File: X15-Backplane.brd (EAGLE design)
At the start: 160 x 100 mm, 34 parts, among them U1 ULN2003AD

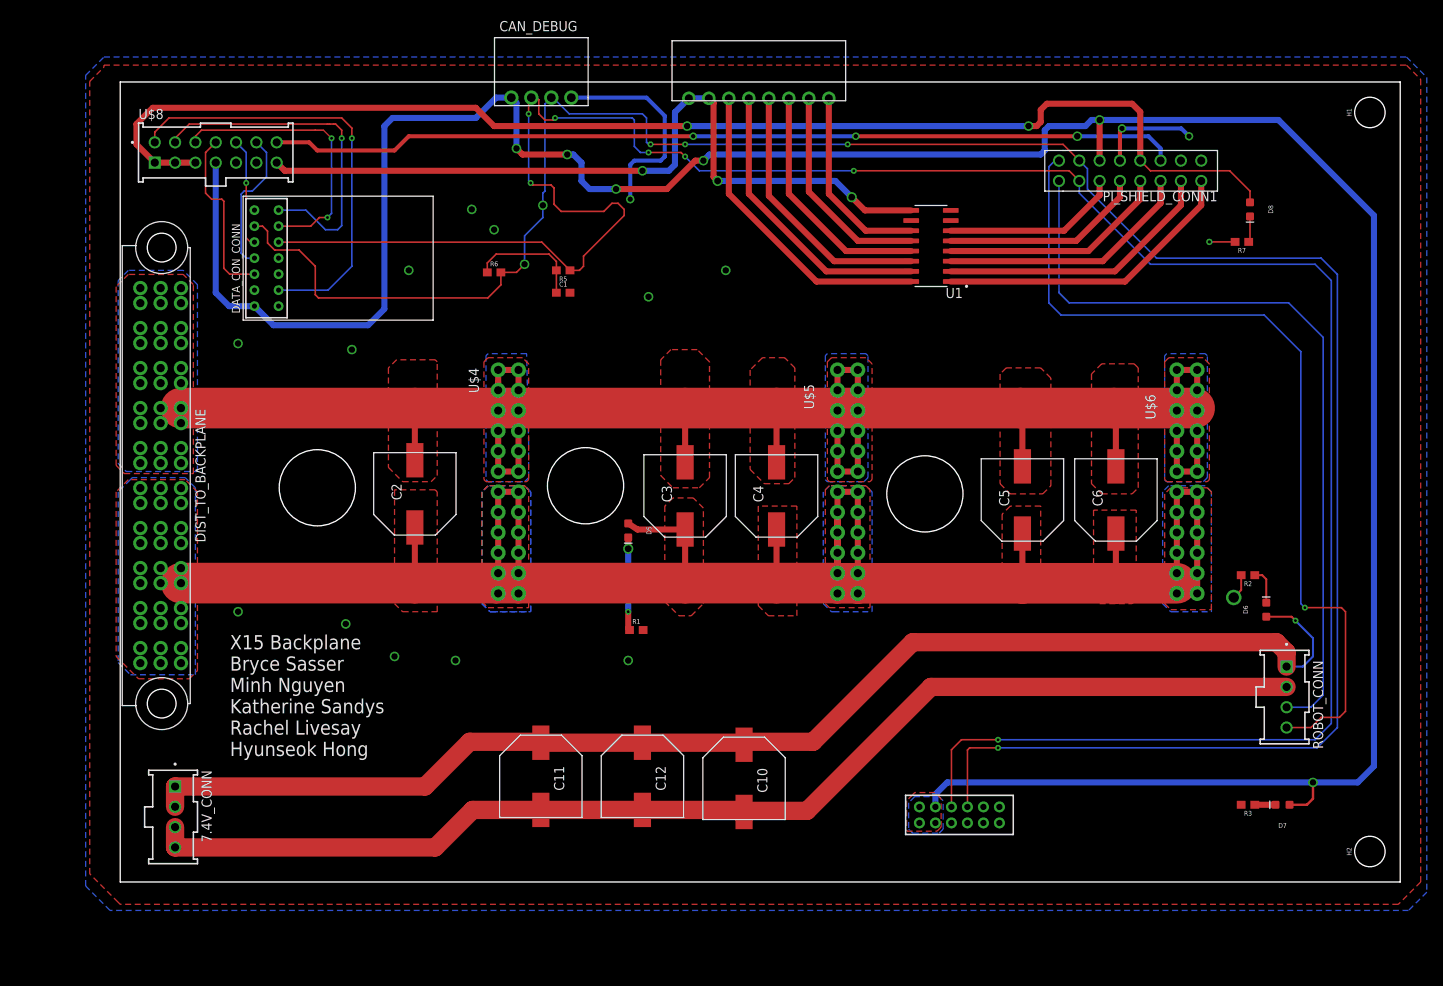
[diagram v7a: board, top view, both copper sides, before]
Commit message: fixed dimensions
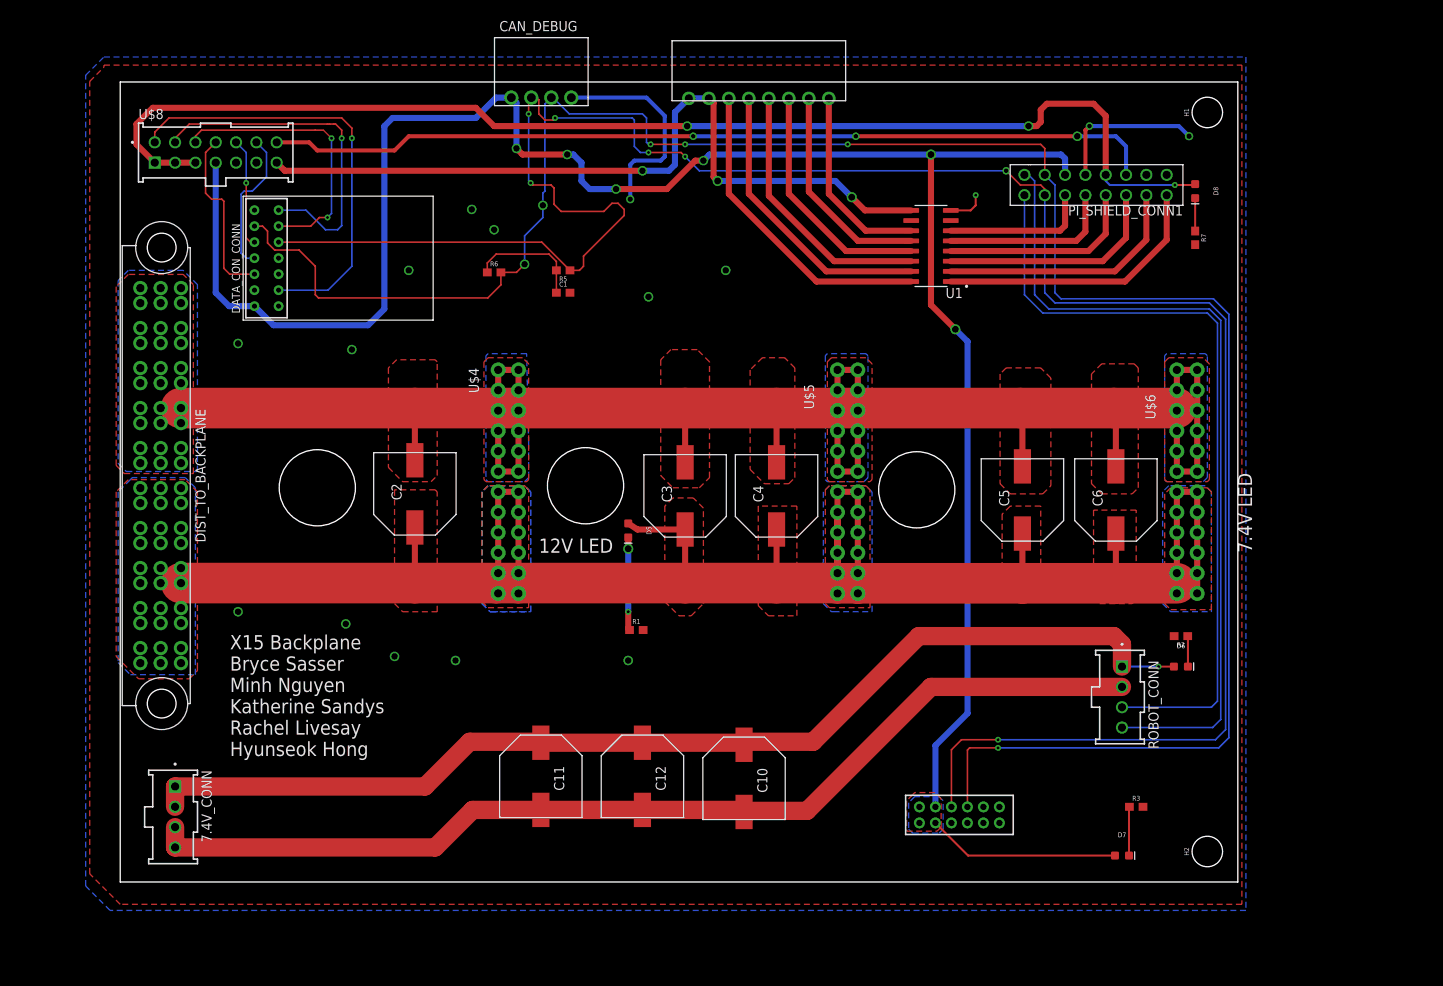
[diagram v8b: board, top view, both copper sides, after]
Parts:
- moved D7 21.0 mm to (125.2, 3.30), turned to 0 degrees
- moved ROBOT_CONN 20.6 mm to (125.2, 23.1)
- moved H1 20.3 mm to (135.9, 96.2)
- moved H2 20.3 mm to (135.9, 3.81)
- moved R3 14.0 mm to (127.0, 9.40), turned to 0 degrees
- moved D6 12.8 mm to (132.6, 26.9), turned to 0 degrees
- moved R2 11.3 mm to (132.6, 30.7)
- moved D8 7.23 mm to (134.4, 86.4)
- moved R7 5.86 mm to (134.4, 80.5), turned to 270 degrees
- moved PI_SHIELD_CONN1 4.67 mm to (132.8, 89.7)
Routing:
- net 3V3: track 344.4 -> 272.0 mm
- net 7.4V: track 164.6 -> 138.7 mm
- net CAN_H: track 299.9 -> 277.8 mm
- net CAN_L: track 287.1 -> 266.2 mm
- net 7.4VGND: track 150.0 -> 129.4 mm
- net ROBOT_ARM_2: track 110.8 -> 103.1 mm, vias 1 -> 0
- net 5V: track 163.4 -> 156.0 mm, vias 2 -> 3
- net GND: track 46.1 -> 50.7 mm, vias 17 -> 16
- net GPIO6: track 22.2 -> 18.4 mm
- net GPIO4: track 28.7 -> 25.1 mm
- net GPIO5: track 25.4 -> 21.9 mm
- net GPIO3: track 32.0 -> 28.5 mm
- net GPIO1: track 38.3 -> 34.7 mm
- net GPIO2: track 35.2 -> 31.7 mm
- net N$3: track 2.59 -> 6.12 mm
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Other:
- board size 160 x 100 mm -> 139.7 x 100 mm
- board text added: "12V LED"
- board text added: "7.4V LED"
